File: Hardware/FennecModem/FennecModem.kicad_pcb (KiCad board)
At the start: 2 copper layers, 75 x 116.7 mm, 30 parts, among them J101 USB_C_Receptacle_USB2.0, J201 Conn_Coaxial, U101 ATmega32U4-A, U201 DRA818V, Y101 16mHz

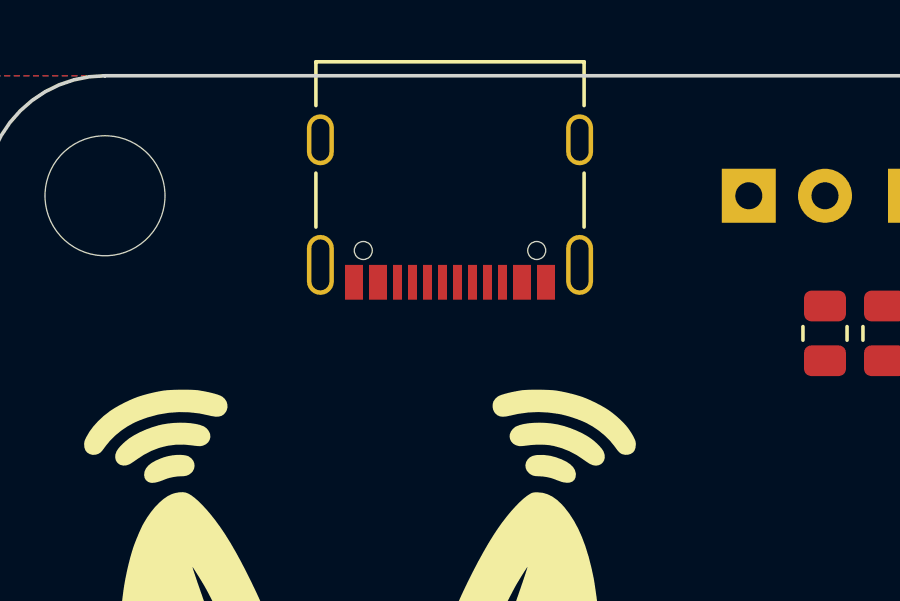
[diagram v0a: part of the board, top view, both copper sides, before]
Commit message: Add USBC
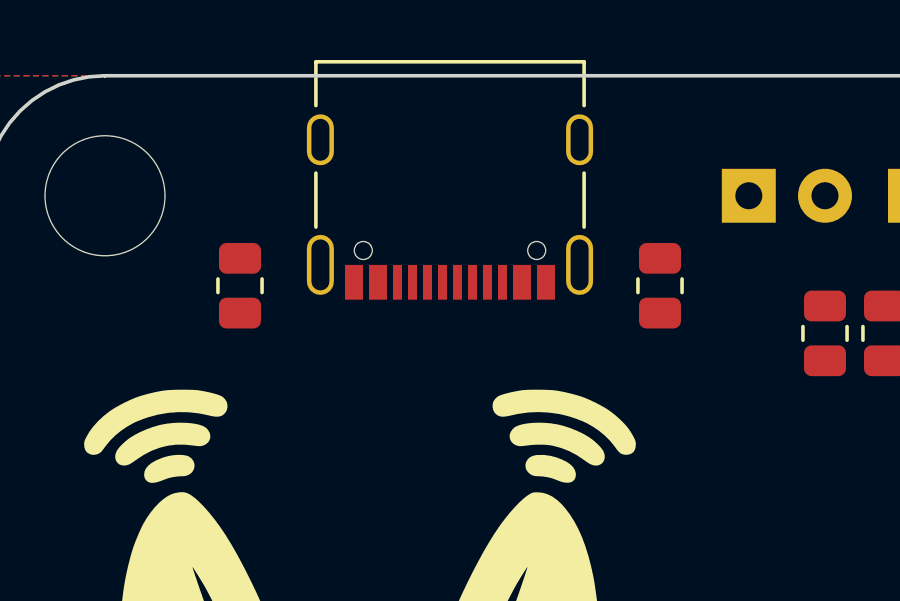
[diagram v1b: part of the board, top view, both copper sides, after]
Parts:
- added R104: 5K1, Resistor_SMD:R_0805_2012Metric, F.Cu at (121.0, 47.0)
- added R105: 5K1, Resistor_SMD:R_0805_2012Metric, F.Cu at (135.0, 47.0)
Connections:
- net Net-(J101-VBUS-PadA4) renamed VBUS
- J101 pad A5: unconnected-(J101-CC1-PadA5) -> Net-(J101-CC1)
- J101 pad A6: /D+ -> /USB+
- J101 pad A7: /D- -> /USB-
- J101 pad B5: unconnected-(J101-CC2-PadB5) -> Net-(J101-CC2)
- J101 pad B6: /D+ -> /USB+
- J101 pad B7: /D- -> /USB-
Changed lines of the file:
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@@
   (net 34 "Net-(FL201-IN)")
   (net 35 "Net-(FL201-OUT)")
-  (net 36 "Net-(J101-VBUS-PadA4)")
-  (net 37 "unconnected-(J101-CC1-PadA5)")
+  (net 36 "VBUS")
+  (net 37 "Net-(J101-CC1)")
   (net 38 "Net-(U101-XTAL1)")
   (net 39 "Net-(U101-XTAL2)")
   (net 40 "unconnected-(J101-SBU1-PadA8)")
-  (net 41 "unconnected-(J101-CC2-PadB5)")
+  (net 41 "/USB+")
   (net 42 "/D+")
   (net 43 "/D-")
@@
   (net 95 "/STAT")
   (net 96 "Net-(D101-A)")
+  (net 97 "/USB-")
+  (net 98 "Net-(J101-CC2)")
   (footprint "Symbol:KiCad-Logo2_5mm_SilkScreen" (layer "F.Cu")
     (at 177 62.5 -90)
@@
   )
   (footprint "Resistor_SMD:R_0805_2012Metric" (layer "F.Cu")
+    (at 121 47 90)
+    (descr "Resistor SMD 0805 (2012 Metric), square (rectangular) end terminal, IPC_7351 nominal, (Body size source: IPC-SM-782 page 72, https://www.pcb-3d.com/wordpress/wp-content/uploads/ipc-sm-782a_amendment_1_and_2.pdf), generated with kicad-footprint-generator")
+    (tags "resistor")
+    (property "LCSC#" "C269748")
+    (property "Sheetfile" "FennecModem.kicad_sch")
+    (property "Sheetname" "")
+    (property "ki_description" "Resistor, small symbol")
+    (property "ki_keywords" "R resistor")
+    (attr smd)
+    (fp_text reference "R104" (at 0 -1.65 90) (layer "F.SilkS") hide
+        (effects (font (size 1 1) (thickness 0.15)))
+    )
+    (fp_text value "5K1" (at 0 1.65 90) (layer "F.Fab")
+        (effects (font (size 1 1) (thickness 0.15)))
+    )
+    (fp_text user "${REFERENCE}" (at 0 0 90) (layer "F.Fab")
+        (effects (font (size 0.5 0.5) (thickness 0.08)))
+    )
+    (fp_line (start -0.227064 -0.735) (end 0.227064 -0.735)
+      (stroke (width 0.12) (type solid)) (layer "F.SilkS"))
+    (fp_line (start -0.227064 0.735) (end 0.227064 0.735)
+      (stroke (width 0.12) (type solid)) (layer "F.SilkS"))
+    (fp_line (start -1.68 -0.95) (end 1.68 -0.95)
+      (stroke (width 0.05) (type solid)) (layer "F.CrtYd"))
+    (fp_line (start -1.68 0.95) (end -1.68 -0.95)
+      (stroke (width 0.05) (type solid)) (layer "F.CrtYd"))
+    (fp_line (start 1.68 -0.95) (end 1.68 0.95)
+      (stroke (width 0.05) (type solid)) (layer "F.CrtYd"))
+    (fp_line (start 1.68 0.95) (end -1.68 0.95)
+      (stroke (width 0.05) (type solid)) (layer "F.CrtYd"))
+    (fp_line (start -1 -0.625) (end 1 -0.625)
+      (stroke (width 0.1) (type solid)) (layer "F.Fab"))
+    (fp_line (start -1 0.625) (end -1 -0.625)
+      (stroke (width 0.1) (type solid)) (layer "F.Fab"))
+    (fp_line (start 1 -0.625) (end 1 0.625)
+      (stroke (width 0.1) (type solid)) (layer "F.Fab"))
+    (fp_line (start 1 0.625) (end -1 0.625)
+      (stroke (width 0.1) (type solid)) (layer "F.Fab"))
+    (pad "1" smd roundrect (at -0.9125 0 90) (size 1.025 1.4) (layers "F.Cu" "F.Paste" "F.Mask") (roundrect_rratio 0.243902)
+      (net 29 "GND") (pintype "passive"))
+    (pad "2" smd roundrect (at 0.9125 0 90) (size 1.025 1.4) (layers "F.Cu" "F.Paste" "F.Mask") (roundrect_rratio 0.243902)
+      (net 98 "Net-(J101-CC2)") (pintype "passive"))
+    (model "${KICAD6_3DMODEL_DIR}/Resistor_SMD.3dshapes/R_0805_2012Metric.wrl"
+      (offset (xyz 0 0 0))
+      (scale (xyz 1 1 1))
+      (rotate (xyz 0 0 0))
+    )
+  )
+  (footprint "Resistor_SMD:R_0805_2012Metric" (layer "F.Cu")
     (at 166.0875 118.75)
     (descr "Resistor SMD 0805 (2012 Metric), square (rectangular) end terminal, IPC_7351 nominal, (Body size source: IPC-SM-782 page 72, https://www.pcb-3d.com/wordpress/wp-content/uploads/ipc-sm-782a_amendment_1_and_2.pdf), generated with kicad-footprint-generator")
@@
       (net 29 "GND") (pinfunction "GND") (pintype "passive"))
     (pad "A4" smd rect (at -2.4 -2.51 180) (size 0.6 1.16) (layers "F.Cu" "F.Paste" "F.Mask")
-      (net 36 "Net-(J101-VBUS-PadA4)") (pinfunction "VBUS") (pintype "passive"))
+      (net 36 "VBUS") (pinfunction "VBUS") (pintype "passive"))
     (pad "A5" smd rect (at -1.25 -2.51) (size 0.3 1.16) (layers "F.Cu" "F.Paste" "F.Mask")
-      (net 37 "unconnected-(J101-CC1-PadA5)") (pinfunction "CC1") (pintype "bidirectional"))
+      (net 37 "Net-(J101-CC1)") (pinfunction "CC1") (pintype "bidirectional"))
     (pad "A6" smd rect (at -0.25 -2.51) (size 0.3 1.16) (layers "F.Cu" "F.Paste" "F.Mask")
-      (net 42 "/D+") (pinfunction "D+") (pintype "bidirectional"))
+      (net 41 "/USB+") (pinfunction "D+") (pintype "bidirectional"))
     (pad "A7" smd rect (at 0.25 -2.51) (size 0.3 1.16) (layers "F.Cu" "F.Paste" "F.Mask")
-      (net 43 "/D-") (pinfunction "D-") (pintype "bidirectional"))
+      (net 97 "/USB-") (pinfunction "D-") (pintype "bidirectional"))
     (pad "A8" smd rect (at 1.25 -2.51) (size 0.3 1.16) (layers "F.Cu" "F.Paste" "F.Mask")
-      (net 40 "unconnected-(J101-SBU1-PadA8)") (pinfunction "SBU1") (pintype "bidirectional"))
+      (net 40 "unconnected-(J101-SBU1-PadA8)") (pinfunction "SBU1") (pintype "bidirectional+no_connect"))
     (pad "A9" smd rect (at 2.4 -2.51 180) (size 0.6 1.16) (layers "F.Cu" "F.Paste" "F.Mask")
-      (net 36 "Net-(J101-VBUS-PadA4)") (pinfunction "VBUS") (pintype "passive"))
+      (net 36 "VBUS") (pinfunction "VBUS") (pintype "passive"))
     (pad "A12" smd rect (at 3.2 -2.51 180) (size 0.6 1.16) (layers "F.Cu" "F.Paste" "F.Mask")
       (net 29 "GND") (pinfunction "GND") (pintype "passive"))
@@
       (net 29 "GND") (pinfunction "GND") (pintype "passive"))
     (pad "B4" smd rect (at 2.4 -2.51 180) (size 0.6 1.16) (layers "F.Cu" "F.Paste" "F.Mask")
-      (net 36 "Net-(J101-VBUS-PadA4)") (pinfunction "VBUS") (pintype "passive"))
+      (net 36 "VBUS") (pinfunction "VBUS") (pintype "passive"))
     (pad "B5" smd rect (at 1.75 -2.51) (size 0.3 1.16) (layers "F.Cu" "F.Paste" "F.Mask")
-      (net 41 "unconnected-(J101-CC2-PadB5)") (pinfunction "CC2") (pintype "bidirectional"))
+      (net 98 "Net-(J101-CC2)") (pinfunction "CC2") (pintype "bidirectional"))
     (pad "B6" smd rect (at 0.75 -2.51) (size 0.3 1.16) (layers "F.Cu" "F.Paste" "F.Mask")
-      (net 42 "/D+") (pinfunction "D+") (pintype "bidirectional"))
+      (net 41 "/USB+") (pinfunction "D+") (pintype "bidirectional"))
     (pad "B7" smd rect (at -0.75 -2.51) (size 0.3 1.16) (layers "F.Cu" "F.Paste" "F.Mask")
-      (net 43 "/D-") (pinfunction "D-") (pintype "bidirectional"))
+      (net 97 "/USB-") (pinfunction "D-") (pintype "bidirectional"))
     (pad "B8" smd rect (at -1.75 -2.51) (size 0.3 1.16) (layers "F.Cu" "F.Paste" "F.Mask")
-      (net 44 "unconnected-(J101-SBU2-PadB8)") (pinfunction "SBU2") (pintype "bidirectional"))
+      (net 44 "unconnected-(J101-SBU2-PadB8)") (pinfunction "SBU2") (pintype "bidirectional+no_connect"))
     (pad "B9" smd rect (at -2.4 -2.51 180) (size 0.6 1.16) (layers "F.Cu" "F.Paste" "F.Mask")
-      (net 36 "Net-(J101-VBUS-PadA4)") (pinfunction "VBUS") (pintype "passive"))
+      (net 36 "VBUS") (pinfunction "VBUS") (pintype "passive"))
     (pad "B12" smd rect (at -3.2 -2.51 180) (size 0.6 1.16) (layers "F.Cu" "F.Paste" "F.Mask")
       (net 29 "GND") (pinfunction "GND") (pintype "passive"))
@@
     )
   )
+  (footprint "Resistor_SMD:R_0805_2012Metric" (layer "F.Cu")
+    (at 135 47 90)
+    (descr "Resistor SMD 0805 (2012 Metric), square (rectangular) end terminal, IPC_7351 nominal, (Body size source: IPC-SM-782 page 72, https://www.pcb-3d.com/wordpress/wp-content/uploads/ipc-sm-782a_amendment_1_and_2.pdf), generated with kicad-footprint-generator")
+    (tags "resistor")
+    (property "LCSC#" "C269748")
+    (property "Sheetfile" "FennecModem.kicad_sch")
+    (property "Sheetname" "")
+    (property "ki_description" "Resistor, small symbol")
+    (property "ki_keywords" "R resistor")
+    (attr smd)
+    (fp_text reference "R105" (at 0 -1.65 90) (layer "F.SilkS") hide
+        (effects (font (size 1 1) (thickness 0.15)))
+    )
+    (fp_text value "5K1" (at 0 1.65 90) (layer "F.Fab")
+        (effects (font (size 1 1) (thickness 0.15)))
+    )
+    (fp_text user "${REFERENCE}" (at 0 0 90) (layer "F.Fab")
+        (effects (font (size 0.5 0.5) (thickness 0.08)))
+    )
+    (fp_line (start -0.227064 -0.735) (end 0.227064 -0.735)
+      (stroke (width 0.12) (type solid)) (layer "F.SilkS"))
+    (fp_line (start -0.227064 0.735) (end 0.227064 0.735)
+      (stroke (width 0.12) (type solid)) (layer "F.SilkS"))
+    (fp_line (start -1.68 -0.95) (end 1.68 -0.95)
+      (stroke (width 0.05) (type solid)) (layer "F.CrtYd"))
+    (fp_line (start -1.68 0.95) (end -1.68 -0.95)
+      (stroke (width 0.05) (type solid)) (layer "F.CrtYd"))
+    (fp_line (start 1.68 -0.95) (end 1.68 0.95)
+      (stroke (width 0.05) (type solid)) (layer "F.CrtYd"))
+    (fp_line (start 1.68 0.95) (end -1.68 0.95)
+      (stroke (width 0.05) (type solid)) (layer "F.CrtYd"))
+    (fp_line (start -1 -0.625) (end 1 -0.625)
+      (stroke (width 0.1) (type solid)) (layer "F.Fab"))
+    (fp_line (start -1 0.625) (end -1 -0.625)
+      (stroke (width 0.1) (type solid)) (layer "F.Fab"))
+    (fp_line (start 1 -0.625) (end 1 0.625)
+      (stroke (width 0.1) (type solid)) (layer "F.Fab"))
+    (fp_line (start 1 0.625) (end -1 0.625)
+      (stroke (width 0.1) (type solid)) (layer "F.Fab"))
+    (pad "1" smd roundrect (at -0.9125 0 90) (size 1.025 1.4) (layers "F.Cu" "F.Paste" "F.Mask") (roundrect_rratio 0.243902)
+      (net 29 "GND") (pintype "passive"))
+    (pad "2" smd roundrect (at 0.9125 0 90) (size 1.025 1.4) (layers "F.Cu" "F.Paste" "F.Mask") (roundrect_rratio 0.243902)
+      (net 37 "Net-(J101-CC1)") (pintype "passive"))
+    (model "${KICAD6_3DMODEL_DIR}/Resistor_SMD.3dshapes/R_0805_2012Metric.wrl"
+      (offset (xyz 0 0 0))
+      (scale (xyz 1 1 1))
+      (rotate (xyz 0 0 0))
+    )
+  )

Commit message: Stop drillin' holes in me ship
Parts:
- R101, R102: value 300 -> ?
- moved R103 5.11 mm to (140.0, 51.0)
- moved R202 5.11 mm to (138.0, 51.0)
- moved R205 5.11 mm to (136.0, 51.0)
- moved J201 0.15 mm to (173.1, 42.5)
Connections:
- net Net-(FL201-IN) renamed /Radio/ANT_OUT
- net Net-(FL201-OUT) renamed /Radio/ANT
- R101 pad 2: /D+ -> /USB+
- R102 pad 2: /D- -> /USB-
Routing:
- net /Radio/ANT_OUT: track 0.00 -> 6.85 mm
- net /Radio/ANT: track 0.00 -> 4.46 mm
- net GND: vias 0 -> 17
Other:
- board text added: "Need to do this math out still, make sure traces are good"

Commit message: Add upstream lib changes and more design
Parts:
- removed C101: EBM15DSEH, KenwoodFox:Lewis_Card_Connector
- added C104: 100nf, Capacitor_SMD:C_0805_2012Metric, F.Cu at (166.7, 114.1)
- added C105: 1uf, Capacitor_SMD:C_0805_2012Metric, F.Cu at (166.7, 117.1)
- added C302: 1μf, Capacitor_SMD:C_0805_2012Metric, F.Cu at (124.3, 146.6)
- added C303: 0.1μf, Capacitor_SMD:C_0805_2012Metric, F.Cu at (127.3, 146.6)
- added D102: SCK, LED_SMD:LED_0805_2012Metric, F.Cu at (171.1, 114.1)
- added D103: MBR0520LT, Diode_SMD:D_SOD-123, F.Cu at (132.0, 51.5)
- added J102: ICSP, Connector:Tag-Connect_TC2030-IDC-FP_2x03_P1.27mm_Vertical, B.Cu at (137.4, 121.5)
- added R106: 10K, Resistor_SMD:R_0805_2012Metric, F.Cu at (125.2, 116.0)
- added R107: 330, Resistor_SMD:R_0805_2012Metric, F.Cu at (171.1, 117.1)
- added SW101: RESET, Button_Switch_THT:SW_PUSH_6mm_H5mm, F.Cu at (125.0, 108.0)
- added U301: NCP1117-12_SOT223, Package_TO_SOT_SMD:SOT-223-3_TabPin2, F.Cu at (118.7, 143.8)
- added U302: ~, KenwoodFox:Lewis_Card_Connector, F.Cu at (150.0, 150.1)
- C102, C103: footprint Capacitor_SMD:C_0805_2012Metric -> Capacitor_SMD:C_0603_1608Metric
- R101, R102: value ? -> 22R
- R103: value 300 -> 330
- moved R101 95.2 mm to (126.0, 50.0), turned to 90 degrees
- moved R102 91.7 mm to (128.0, 50.0), turned to 90 degrees
- moved C103 35.0 mm to (141.5, 132.5), turned to 135 degrees
- moved C102 32.4 mm to (144.0, 135.0), turned to -45 degrees
- moved Y101 23.5 mm to (140.0, 137.0), turned to -45 degrees
- moved C201 8.00 mm to (166.7, 122.1)
- moved C202 8.00 mm to (166.7, 125.1)
- moved R201 8.00 mm to (171.1, 122.0)
- moved R206 8.00 mm to (171.1, 125.0)
- moved G*** 3.75 mm to (125.0, 65.5) (x2)
- turned U101 to -45 degrees
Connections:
- net VBUS renamed Net-(D103-A)
- U101 pad 10: unconnected-(U101-PB2-Pad10) -> /SDO
- U101 pad 11: unconnected-(U101-PB3-Pad11) -> /SDI
- U101 pad 13: unconnected-(U101-~{RESET}-Pad13) -> /RESET
- U101 pad 14: Net-(U101-VCC-Pad14) -> +5V
- U101 pad 2: unconnected-(U101-UVCC-Pad2) -> +5V
- U101 pad 24: Net-(U101-AVCC-Pad24) -> +5V
- U101 pad 34: Net-(U101-VCC-Pad14) -> +5V
- U101 pad 42: unconnected-(U101-AREF-Pad42) -> /AREF
- U101 pad 44: Net-(U101-AVCC-Pad24) -> +5V
- U101 pad 6: unconnected-(U101-UCAP-Pad6) -> Net-(U101-UCAP)
- U101 pad 9: unconnected-(U101-PB1-Pad9) -> /SCK
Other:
- board text added: "→"
